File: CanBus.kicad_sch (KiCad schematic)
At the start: 12 parts, among them J2 CAN INPUT, U2 SN65HVD230DR

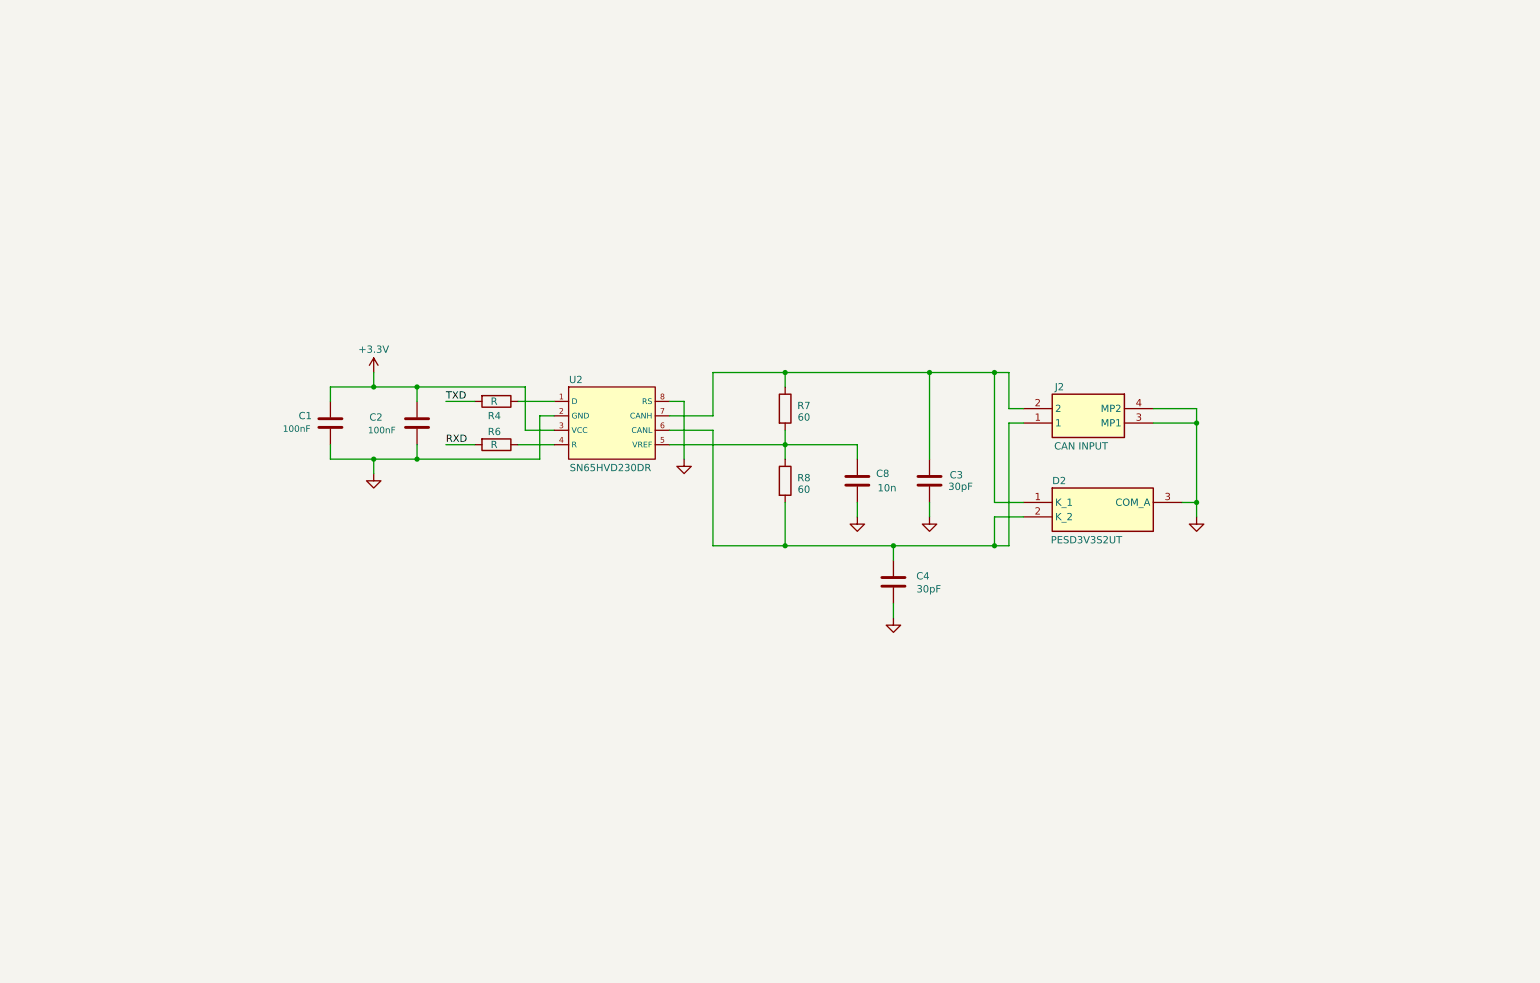
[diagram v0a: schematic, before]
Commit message: Added the Pins for the MCU
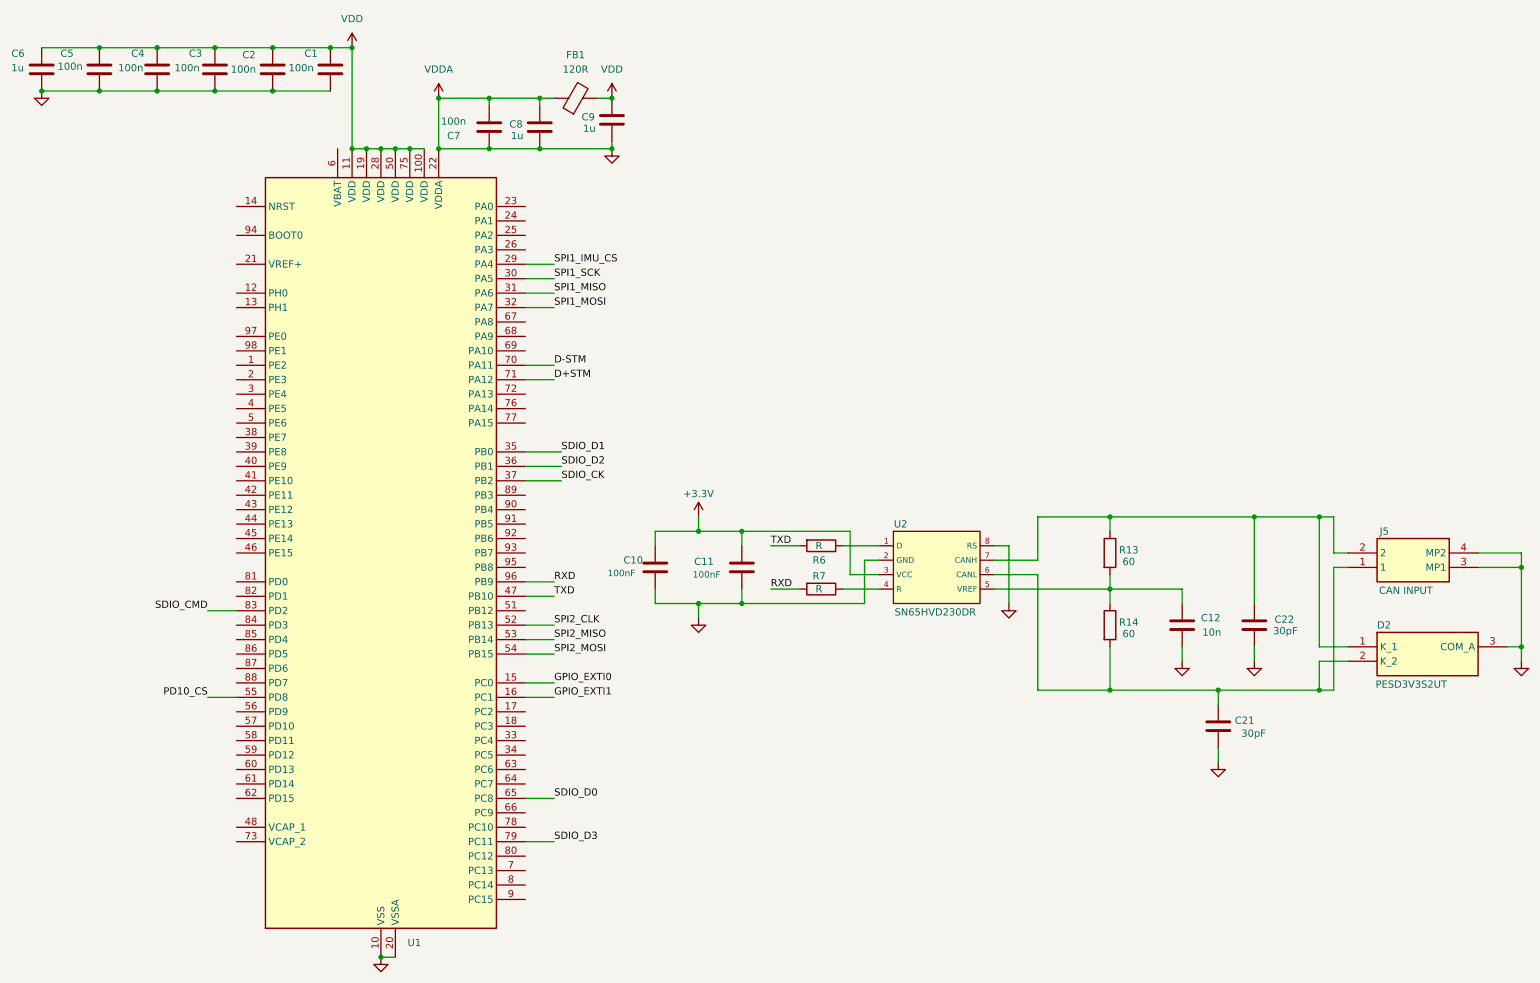
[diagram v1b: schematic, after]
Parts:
- removed J2: CAN INPUT, B2BPHSM4TBTLFSN, symbol SamacSys_Parts:B2B-PH-SM4-TBT_LF__SN_
- removed R4: R, symbol Device:R
- removed R8: 60, symbol Device:R
- added C10, C11: 100nF, symbol Device:C
- added C12: 10n, symbol Device:C
- added C21, C22: 30pF, symbol Device:C
- added C5, C7: 100n, symbol Device:C
- added C6, C9: 1u, symbol Device:C
- added FB1: 120R, symbol Device:FerriteBead
- added J5: CAN INPUT, B2BPHSM4TBTLFSN, symbol SamacSys_Parts:B2B-PH-SM4-TBT_LF__SN_
- added R13, R14: 60, symbol Device:R
- added U1: STM32F446VETx, Package_QFP:LQFP-100_14x14mm_P0.5mm, symbol MCU_ST_STM32F4:STM32F446VETx
- C1, C2: value 100nF -> 100n
- C3, C4: value 30pF -> 100n
- C8: value 10n -> 1u
- R7: value 60 -> R
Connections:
- net +3.3V: now also C10.1, C11.1; no longer C1.1, C2.1
- net GND: now also C3.2, C4.2, C8.1, C10.2, C11.2, C12.2, C21.1, C22.1, C5.2, C6.2, C7.1, C7.2, C9.2, FB1.1, J5.3 (MP1), J5.4 (MP2), U1.10 (VSS), U1.20 (VSSA), U1.22 (VDDA), U1.27 (VSS), U1.49 (VSS), U1.74 (VSS), U1.99 (VSS); no longer C3.1, C4.1
- net RXD: now also R7.2, U1.96 (PB9); no longer R6.2
- net TXD: now also R6.2, U1.47 (PB10)
- net at U2.4 (R): now also R7.1; no longer R6.1
- net at D2.1 (K_1), U2.7 (CANH): now also C22.2, J5.2, R13.1; no longer C3.2, R7.1
- net at D2.2 (K_2), U2.6 (CANL): now also C21.2, J5.1, R14.2; no longer C4.2
- net at U2.1 (D): now also R6.1
- new net: C12.1, R13.2, R14.1, U2.5 (VREF)
- new net D+STM: U1.71 (PA12)
- new net D-STM: U1.70 (PA11)
- new net GPIO_EXTI0: U1.15 (PC0)
- new net GPIO_EXTI1: U1.16 (PC1)
- new net PD10_CS: U1.55 (PD8)
- new net SDIO_CK: U1.37 (PB2)
- new net SDIO_CMD: U1.83 (PD2)
- new net SDIO_D0: U1.65 (PC8)
- new net SDIO_D1: U1.35 (PB0)
- new net SDIO_D2: U1.36 (PB1)
- new net SDIO_D3: U1.79 (PC11)
- new net SPI1_IMU_CS: U1.29 (PA4)
- new net SPI1_MISO: U1.31 (PA6)
- new net SPI1_MOSI: U1.32 (PA7)
- new net SPI1_SCK: U1.30 (PA5)
- new net SPI2_CLK: U1.52 (PB13)
- new net SPI2_MISO: U1.53 (PB14)
- new net SPI2_MOSI: U1.54 (PB15)
- new net VDD: C1.1, C2.1, C3.1, C4.1, C5.1, C6.1, C9.1, FB1.2, U1.100 (VDD), U1.11 (VDD), U1.19 (VDD), U1.28 (VDD), U1.50 (VDD), U1.75 (VDD)
